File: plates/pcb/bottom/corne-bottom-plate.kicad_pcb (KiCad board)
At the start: 2 copper layers, 133.8 x 91.4 mm, 7 parts

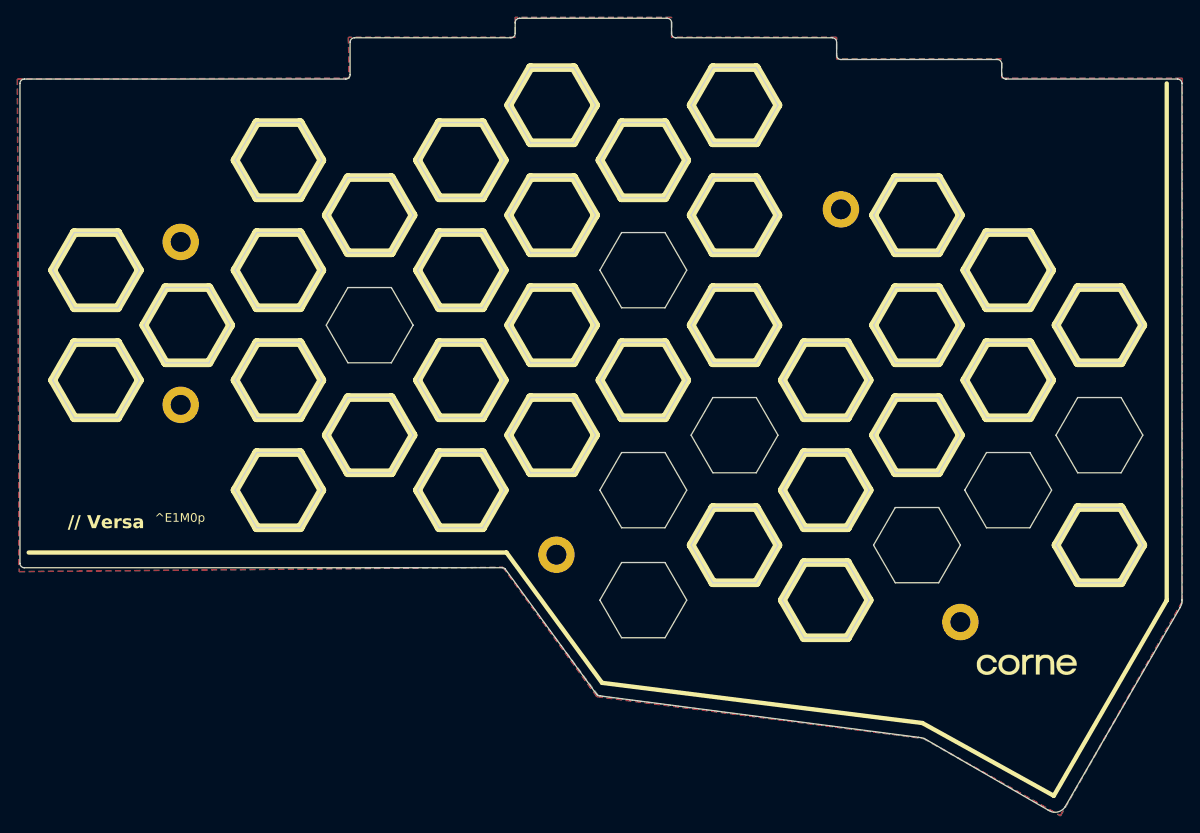
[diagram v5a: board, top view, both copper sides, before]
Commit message: Logo relocated
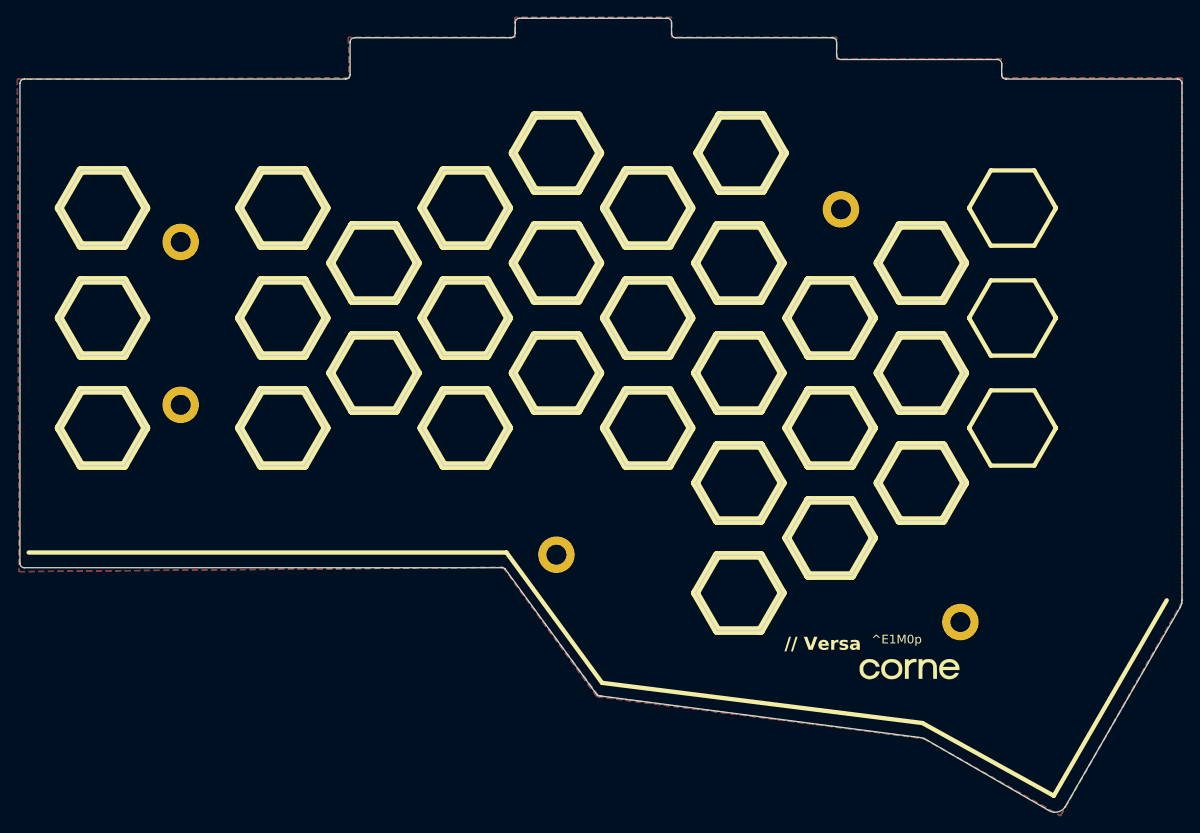
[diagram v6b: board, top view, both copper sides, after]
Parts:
- moved G*** 13.5 mm to (163.5, 136.0) (x2)
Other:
- outline, holes or cut-outs redrawn
